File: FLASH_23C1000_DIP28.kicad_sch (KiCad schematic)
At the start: 8 parts

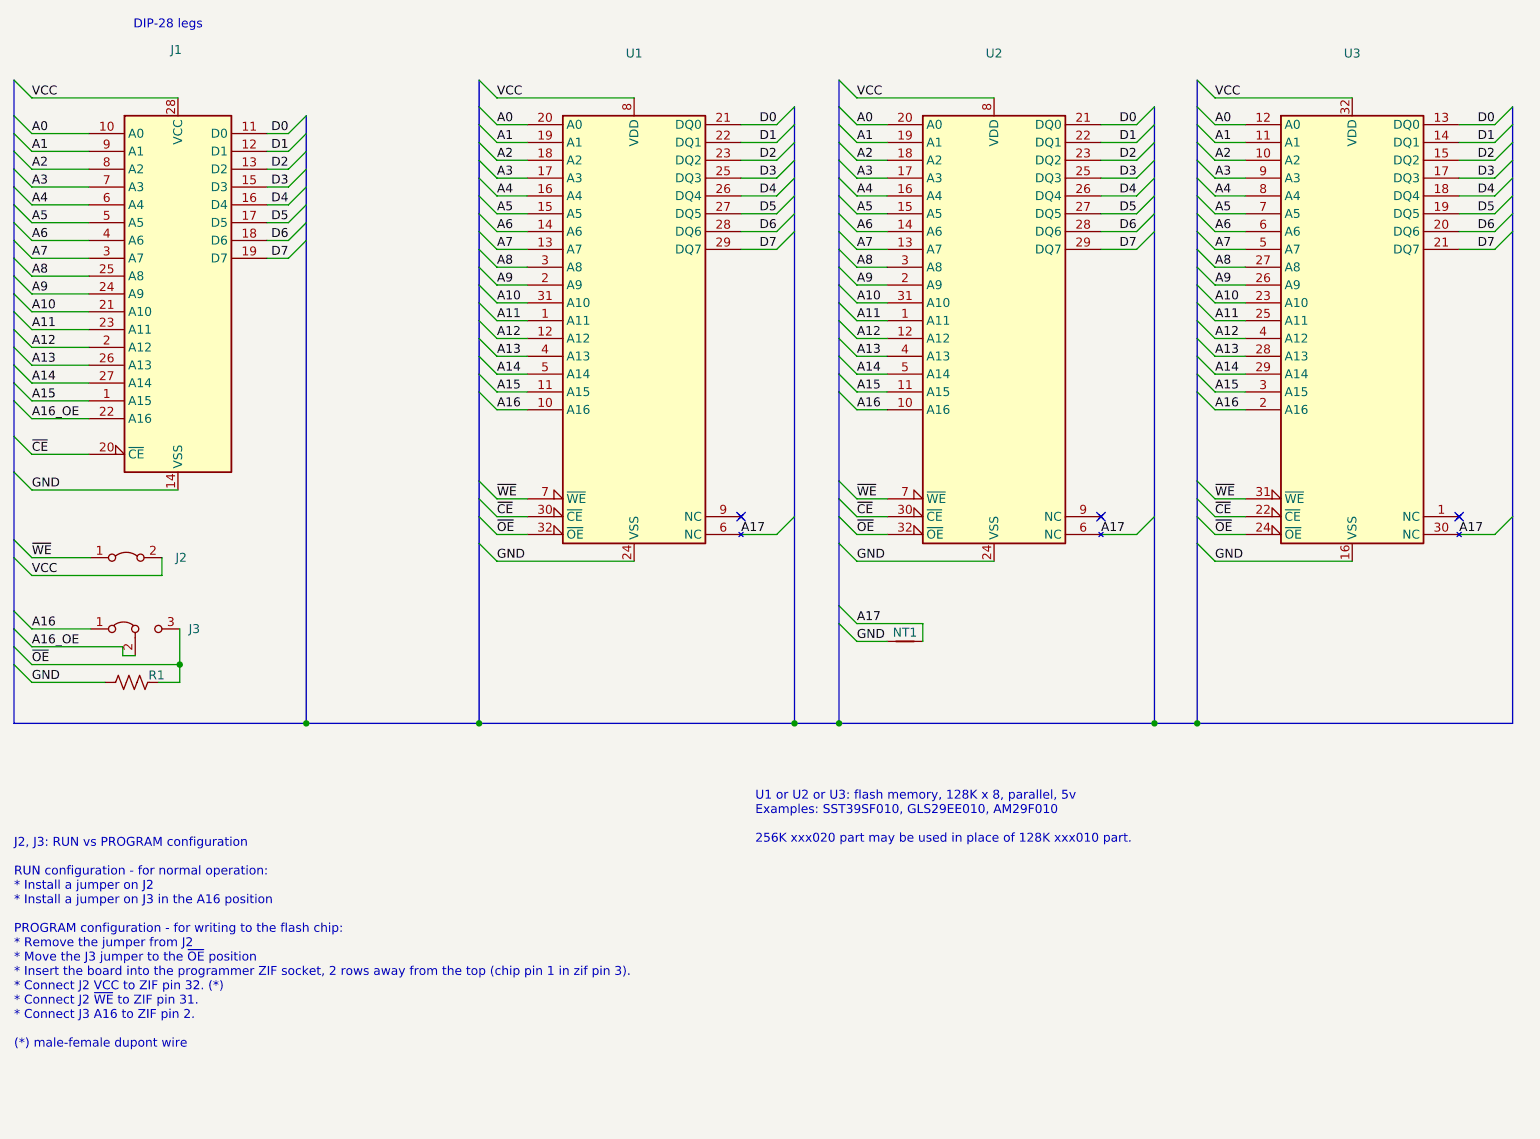
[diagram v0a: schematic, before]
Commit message: Fix wrong pinout on FlashROM_100 TSOPgit add -A!
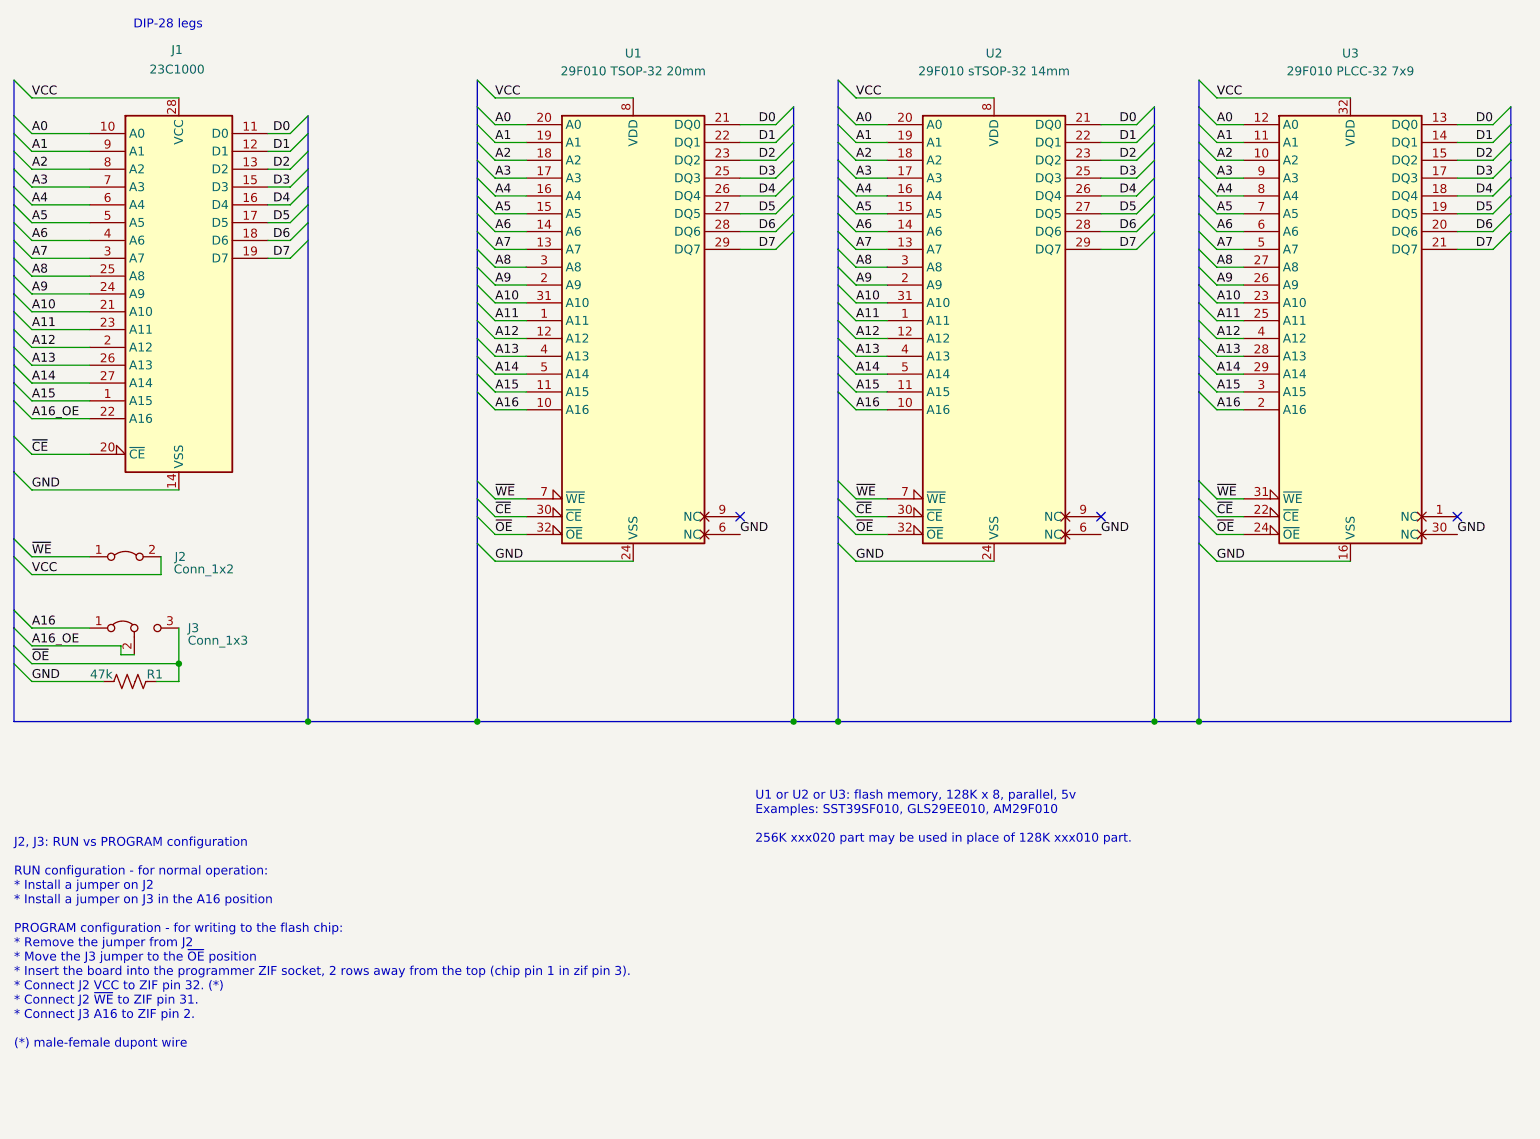
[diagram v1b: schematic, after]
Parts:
- removed NT1: (no value), symbol 000_LOCAL:Net-Tie_2
- J1: value (none) -> 23C1000; footprint (none) -> 000_LOCAL:DIP28_0.6_pcb_sil_pins
- J2: value (none) -> Conn_1x2; footprint (none) -> 000_LOCAL:Pin_Header_Angled_1x02_Pitch2.54mm_shorted
- J3: value (none) -> Conn_1x3; footprint (none) -> 000_LOCAL:Pin_Header_Angled_1x03_Pitch2.54mm_12shorted
- R1: value (none) -> 47k; footprint (none) -> 000_LOCAL:R_0805
- U1: value (none) -> 29F010 TSOP-32 20mm; footprint (none) -> 000_LOCAL:TSOP32-20mm
- U2: value (none) -> 29F010 sTSOP-32 14mm; footprint (none) -> 000_LOCAL:TSOP32-14mm
- U3: value (none) -> 29F010 PLCC-32 7x9; footprint (none) -> 000_LOCAL:PLCC32_7x9
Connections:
- net A17 is gone; now on net GND: U1.6 (NC), U2.6 (NC), U3.30 (NC)

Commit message: 23C100 DIP28 outline, gnd, silk
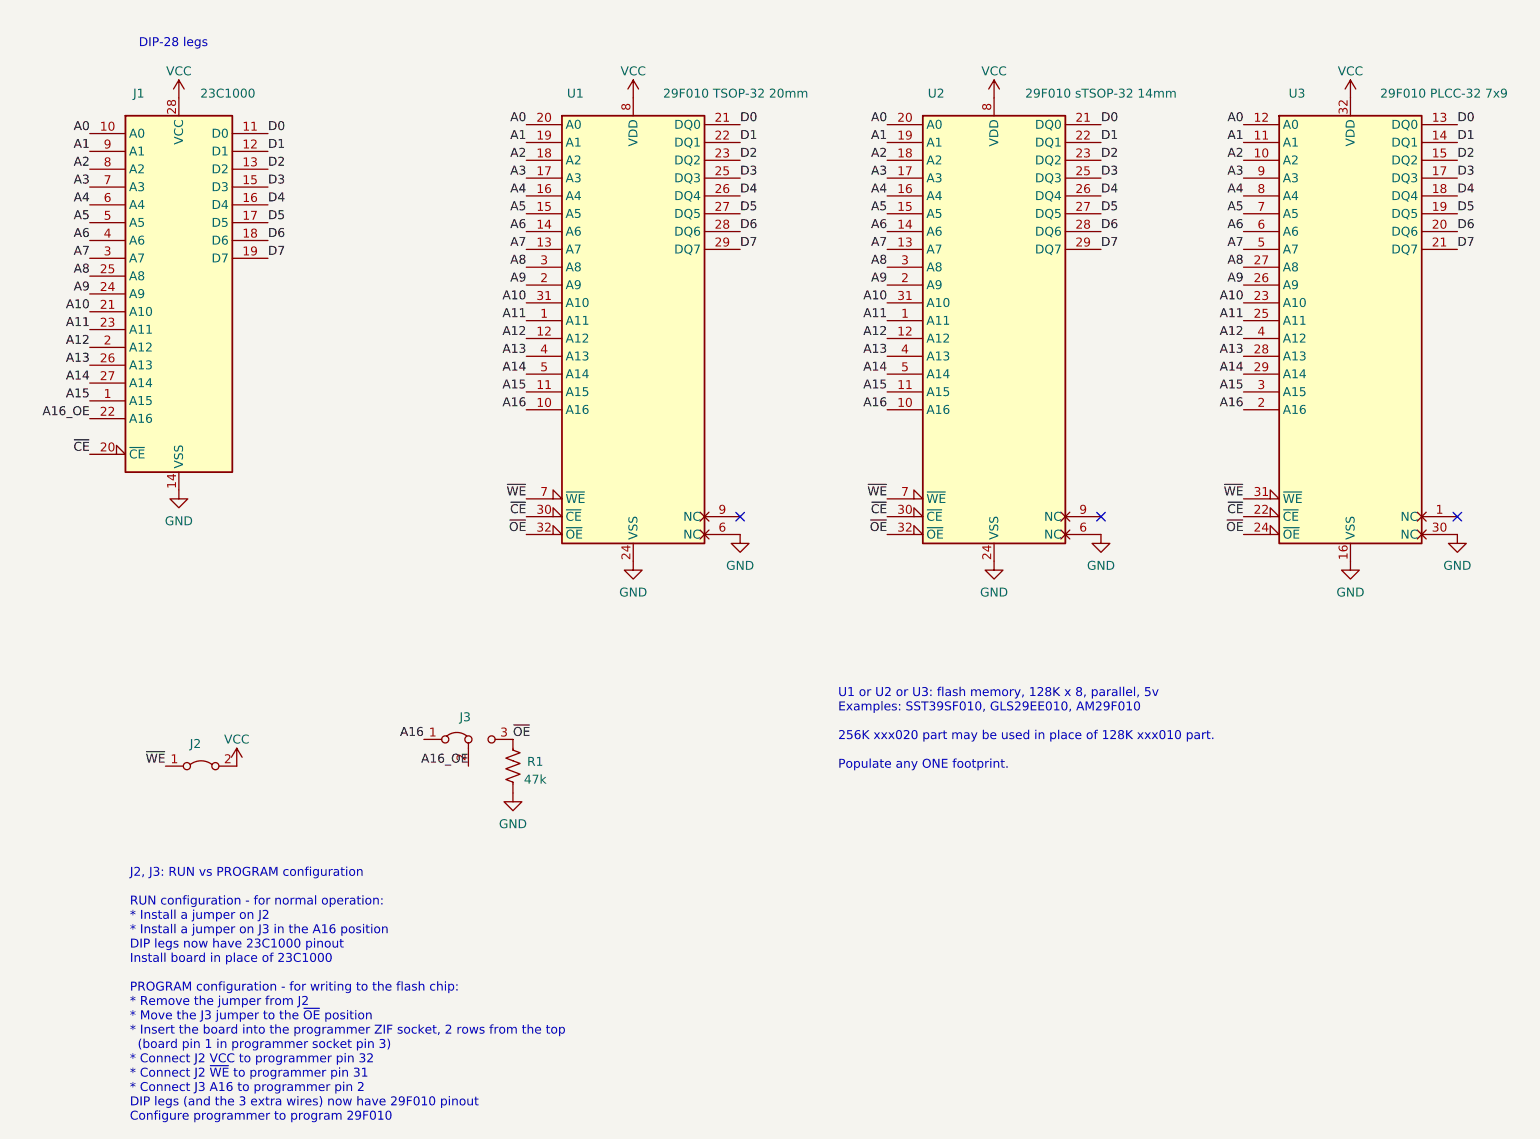
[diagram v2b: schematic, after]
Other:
- note added: "J2, J3: RUN vs PROGRAM configuration RUN configuration - for normal operation: * Install a jumper on J2 * Install a jumper on J3 in the A16 position DIP legs now have 23C1000 pinout Install board in place of 23C1000 PROGRAM configuration - for writing to the flash chip: * Remove the jumper from J2 * Move the J3 jumper to the ~{OE} position * Insert the board into the programmer ZIF socket, 2 rows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"
- note added: "U1 or U2 or U3: flash memory, 128K x 8, parallel, 5v Examples: SST39SF010, GLS29EE010, AM29F010 256K xxx020 part may be used in place of 128K xxx010 part. Populate any ONE footprint."
- note removed: "J2, J3: RUN vs PROGRAM configuration RUN configuration - for normal operation: * Install a jumper on J2 * Install a jumper on J3 in the A16 position PROGRAM configuration - for writing to the flash chip: * Remove the jumper from J2 * Move the J3 jumper to the ~{OE} position * Insert the board into the programmer ZIF socket, 2 rows away from the top (chip pin 1 in zif pin 3). * Connect J2 VCC to Z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"
- note removed: "U1 or U2 or U3: flash memory, 128K x 8, parallel, 5v Examples: SST39SF010, GLS29EE010, AM29F010 256K xxx020 part may be used in place of 128K xxx010 part."
- moved on the sheet: J2, J3, R1

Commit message: dual tsop footprint on flash_23c100_dip28
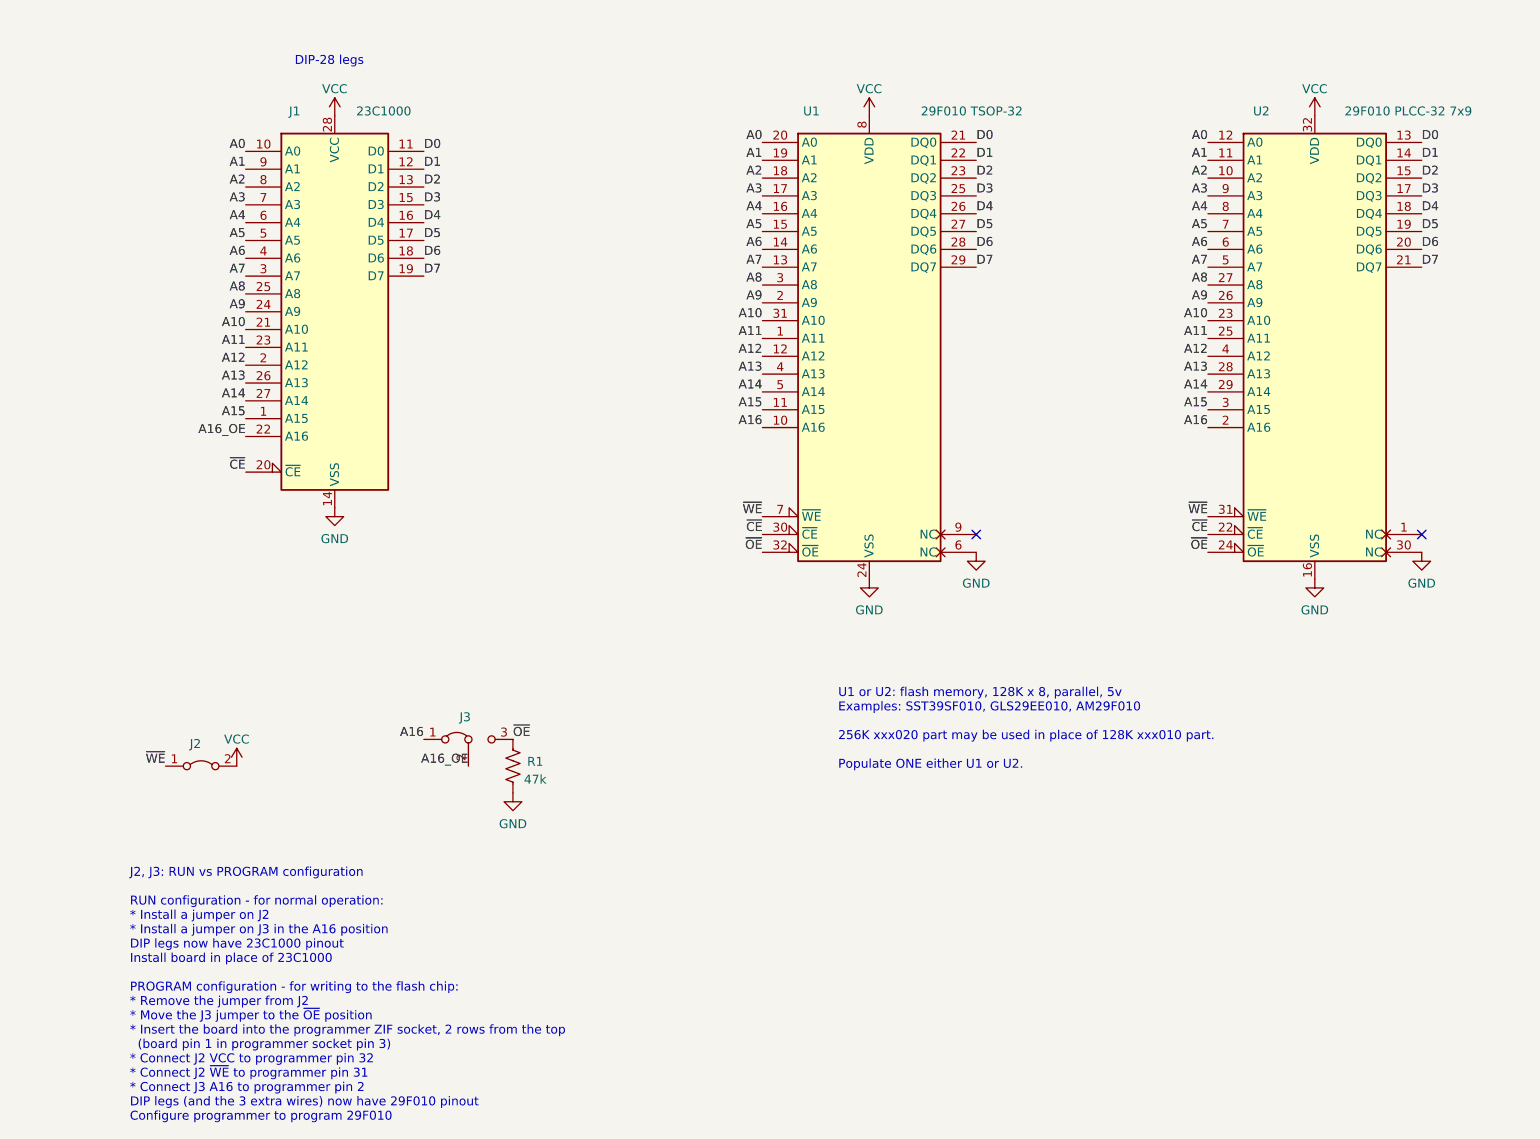
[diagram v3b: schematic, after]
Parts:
- removed U2: 29F010 sTSOP-32 14mm, 000_LOCAL:TSOP32-14mm, symbol 000_LOCAL:SST39SF010_TSOP
- U1: value 29F010 TSOP-32 20mm -> 29F010 TSOP-32; footprint 000_LOCAL:TSOP32-20mm -> 000_LOCAL:TSOP32-dual
- renumbered U3 to U2
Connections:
- no-connect marks 3 -> 2
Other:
- note added: "U1 or U2: flash memory, 128K x 8, parallel, 5v Examples: SST39SF010, GLS29EE010, AM29F010 256K xxx020 part may be used in place of 128K xxx010 part. Populate ONE either U1 or U2."
- note removed: "U1 or U2 or U3: flash memory, 128K x 8, parallel, 5v Examples: SST39SF010, GLS29EE010, AM29F010 256K xxx020 part may be used in place of 128K xxx010 part. Populate any ONE footprint."
- moved on the sheet: J1, U1, U2

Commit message: 23C1000 DIP-28 tsop-32 daul footprint & teardrops
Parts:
- J1: footprint 000_LOCAL:DIP28_0.6_pcb_sil_pins -> 000_LOCAL:DIP-28_600_pcb_shallow_notch
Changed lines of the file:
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@@
       (effects (font (size 1.27 1.27)))
     )
-    (property "Footprint" "000_LOCAL:DIP28_0.6_pcb_sil_pins" (at 76.2 68.58 0)
+    (property "Footprint" "000_LOCAL:DIP-28_600_pcb_shallow_notch" (at 76.2 68.58 0)
       (effects (font (size 1.27 1.27)) hide)
     )
